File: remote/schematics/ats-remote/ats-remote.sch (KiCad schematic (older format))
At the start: 34 parts, among them J1 PWR, J2 ICSP, J3 Conn_01x04_Male, J4 Conn_01x02_Male, U1 RFM95W-915S2, U2 PIC18F06Q40, U3 YIC71009EBGG

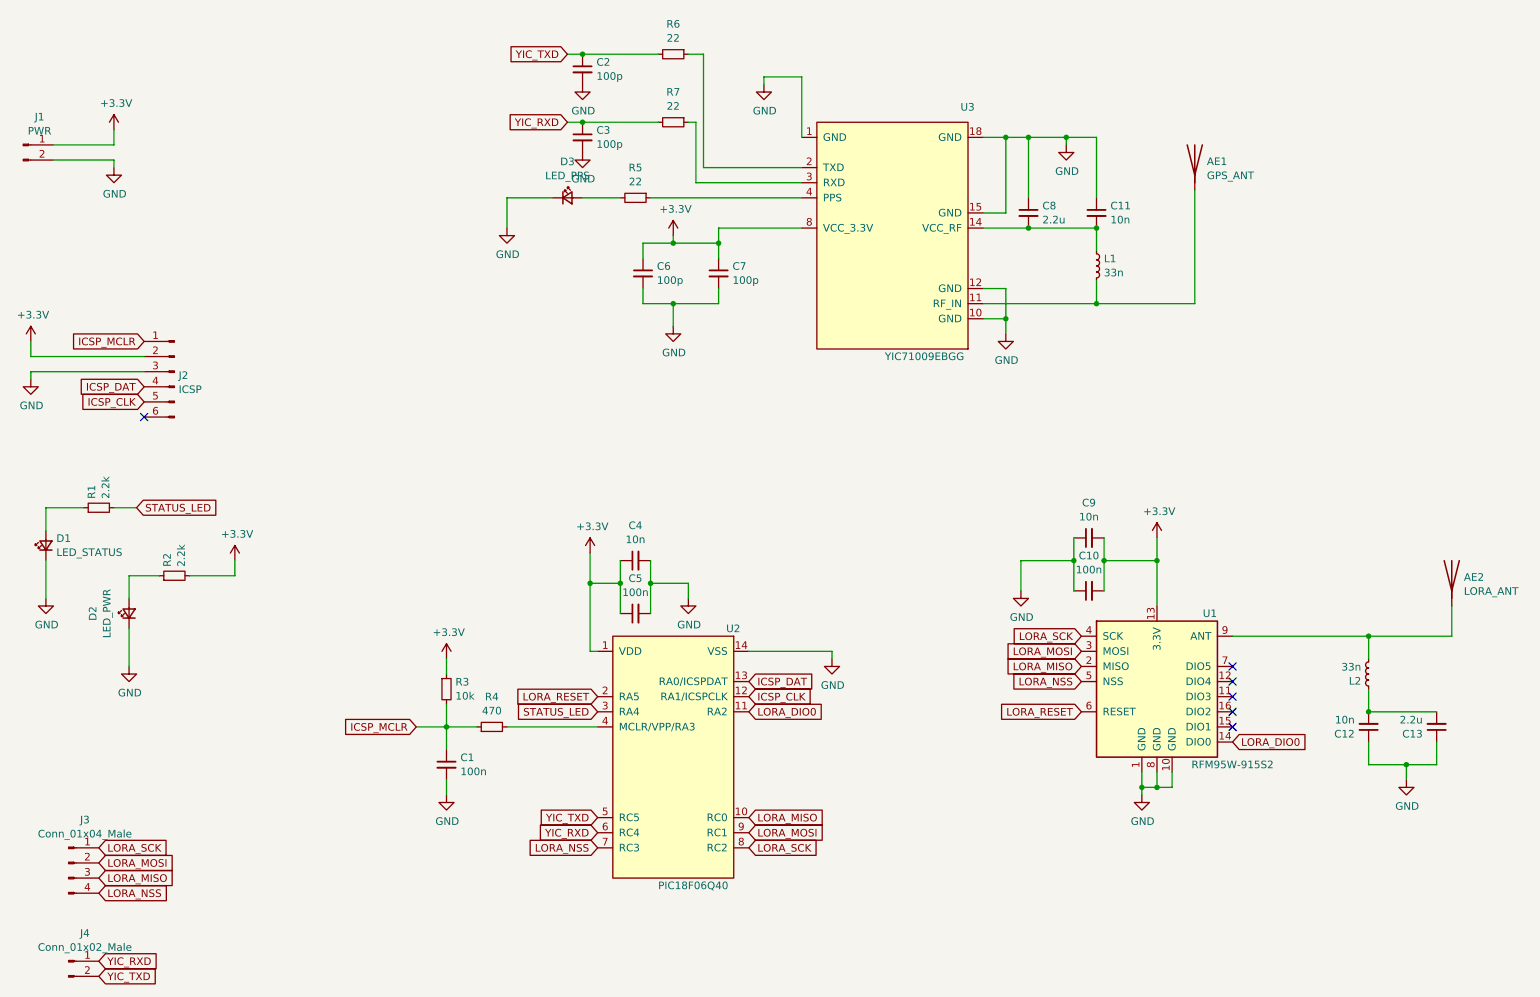
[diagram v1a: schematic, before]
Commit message: v0.2.1 (#3)
* add footprints for gps and lora antennas; start work on new board

* update schematic and pcb to v0.2.0

* Update README.md

* remove gerber files

* update schematic and pcb

* add silk screen

* update silk screen

* fix lora nss via and gps ant grounds
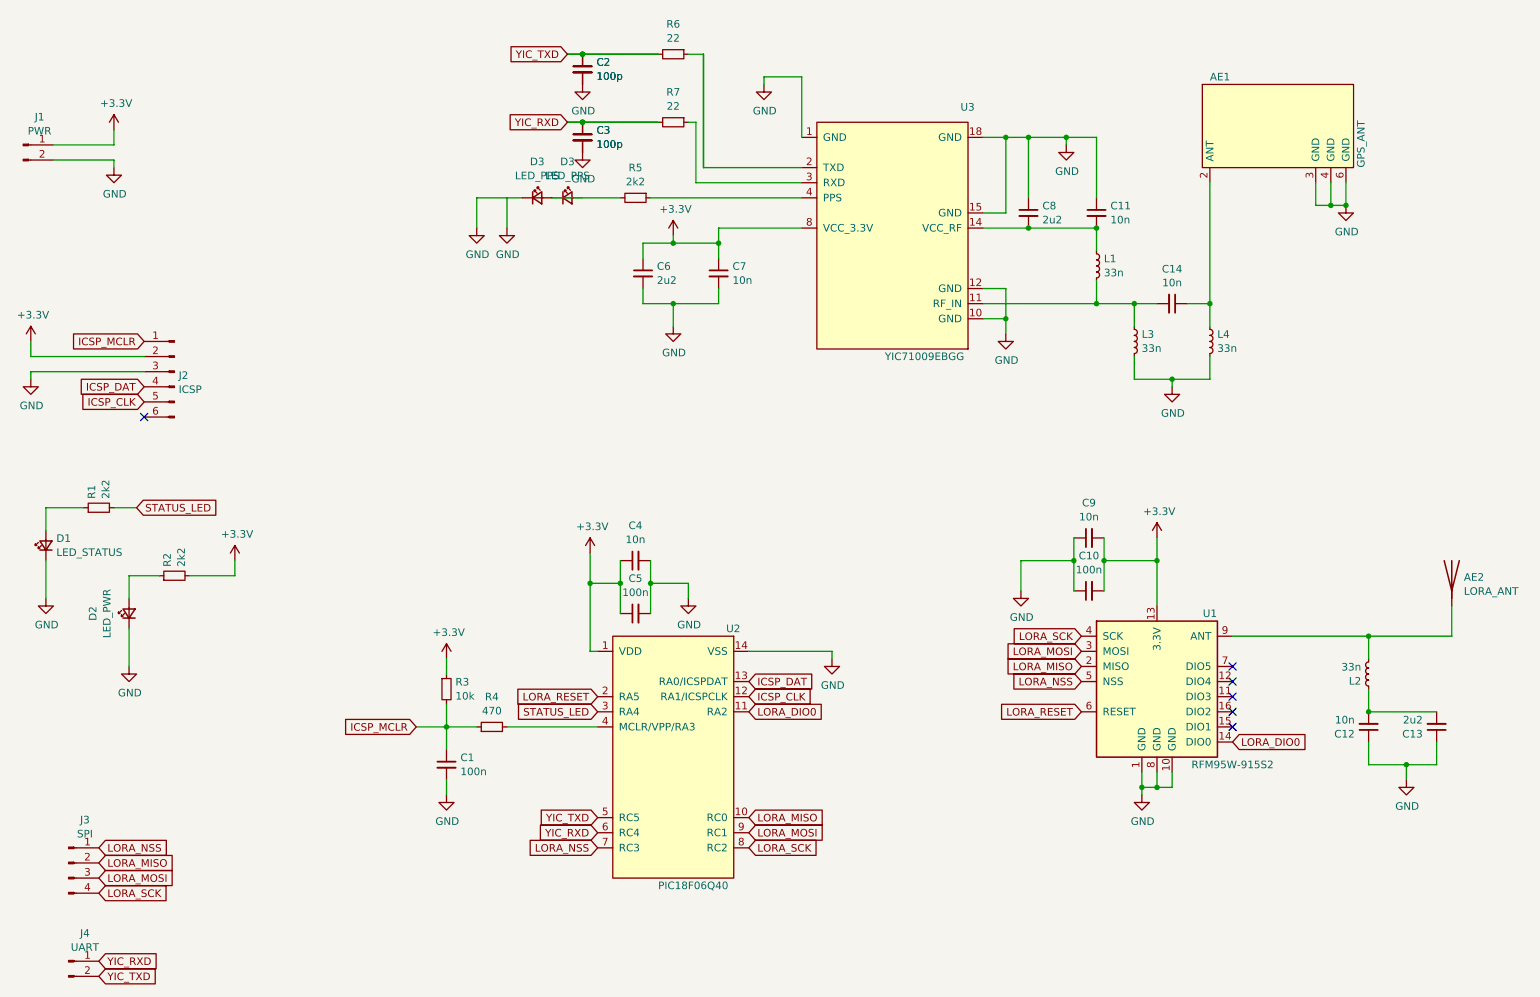
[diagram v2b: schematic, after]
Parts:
- removed AE1: GPS_ANT, ats-remote:GPS_ANT_SR4G008, symbol Device:Antenna
- removed D3: LED_PPS, Diode_SMD:D_1206_3216Metric_Pad1.42x1.75mm_HandSolder, symbol Device:LED_Small
- added AE1: GPS_ANT, ats-remote:GPS_ANT_SR4G008, symbol ats-remote:ACAG1204-915-T
- added C14: 10n, Capacitor_SMD:C_0805_2012Metric_Pad1.18x1.45mm_HandSolder, symbol Device:C_Small
- added D3 (x2): LED_PPS, Diode_SMD:D_1206_3216Metric_Pad1.42x1.75mm_HandSolder, symbol Device:LED_Small
- added L3, L4: 33n, Inductor_SMD:L_0603_1608Metric_Pad1.05x0.95mm_HandSolder, symbol Device:L_Small
- C13, C8: value 2.2u -> 2u2
- C6: value 100p -> 2u2
- C7: value 100p -> 10n
- J3: value Conn_01x04_Male -> SPI
- J4: value Conn_01x02_Male -> UART
- R1, R2: value 2.2k -> 2k2
- R5: value 22 -> 2k2
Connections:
- net GND: now also AE1.3 (GND), AE1.4 (GND), AE1.6 (GND), D3.1 (K), L3.2, L4.2
- net LORA_MISO: now also J3.2 (Pin_2); no longer J3.3 (Pin_3)
- net LORA_MOSI: now also J3.3 (Pin_3); no longer J3.2 (Pin_2)
- net LORA_NSS: now also J3.1 (Pin_1); no longer J3.4 (Pin_4)
- net LORA_SCK: now also J3.4 (Pin_4); no longer J3.1 (Pin_1)
- net at L1.2, U3.11 (RF_IN): now also C14.2, L3.1
- net at R5.2: now also D3.1 (K), D3.2 (A)
- new net: AE1.2 (ANT), C14.1, L4.1
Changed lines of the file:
@@
 	10100 4750 10100 4550
-$Comp
-L Device:Antenna AE1
-U 1 1 61DAE6EE
-P 8400 1600
-F 0 "AE1" H 8480 1590 50  0000 L CNN
-F 1 "GPS_ANT" H 8480 1497 50  0000 L CNN
-F 2 "ats-remote:GPS_ANT_SR4G008" H 8400 1600 50  0001 C CNN
-F 3 "~" H 8400 1600 50  0001 C CNN
-	1    8400 1600
-	1    0    0    -1
-$EndComp
 $Comp
 L Device:LED_Small D1
@@
 P 1150 3900
 F 0 "R1" H 1209 3947 50  0000 L CNN
-F 1 "2.2k" H 1209 3854 50  0000 L CNN
+F 1 "2k2" H 1209 3854 50  0000 L CNN
 F 2 "Resistor_SMD:R_1206_3216Metric_Pad1.30x1.75mm_HandSolder" H 1150 3900 50  0001 C CNN
 F 3 "~" H 1150 3900 50  0001 C CNN
@@
 P 1650 4350
 F 0 "R2" H 1709 4397 50  0000 L CNN
-F 1 "2.2k" H 1709 4304 50  0000 L CNN
+F 1 "2k2" H 1709 4304 50  0000 L CNN
 F 2 "Resistor_SMD:R_1206_3216Metric_Pad1.30x1.75mm_HandSolder" H 1650 4350 50  0001 C CNN
 F 3 "~" H 1650 4350 50  0001 C CNN
@@
 P 7300 1950
 F 0 "C8" H 7392 1997 50  0000 L CNN
-F 1 "2.2u" H 7392 1904 50  0000 L CNN
+F 1 "2u2" H 7392 1904 50  0000 L CNN
 F 2 "Capacitor_SMD:C_0805_2012Metric_Pad1.18x1.45mm_HandSolder" H 7300 1950 50  0001 C CNN
 F 3 "~" H 7300 1950 50  0001 C CNN
@@
 Wire Wire Line
 	7750 1450 7750 1850
-Wire Wire Line
-	8400 1800 8400 2550
 Wire Wire Line
 	7000 2550 7750 2550
@@
 Wire Wire Line
 	7750 2400 7750 2550
-Connection ~ 7750 2550
-Wire Wire Line
-	7750 2550 8400 2550
 Wire Wire Line
 	5800 1750 5100 1750
@@
 P 4700 1850
 F 0 "R5" V 4501 1850 50  0000 C CNN
-F 1 "22" V 4594 1850 50  0000 C CNN
+F 1 "2k2" V 4594 1850 50  0000 C CNN
 F 2 "Resistor_SMD:R_1206_3216Metric_Pad1.30x1.75mm_HandSolder" H 4700 1850 50  0001 C CNN
 F 3 "~" H 4700 1850 50  0001 C CNN
@@
 	0    1    1    0
 $EndComp
+Wire Wire Line
+	5150 900  5150 1650
+Wire Wire Line
+	4850 1350 4350 1350
+Wire Wire Line
+	4850 900  4350 900
+$Comp
+L power:GND #PWR0120
+U 1 1 61F19544
+P 3850 2050
+F 0 "#PWR0120" H 3850 1800 50  0001 C CNN
+F 1 "GND" H 3855 1875 50  0000 C CNN
+F 2 "" H 3850 2050 50  0001 C CNN
+F 3 "" H 3850 2050 50  0001 C CNN
+	1    3850 2050
+	1    0    0    -1
+$EndComp
+$Comp
+L Device:LED_Small D3
+U 1 1 61F1DC27
+P 4250 1850
+F 0 "D3" H 4250 2089 50  0000 C CNN
+F 1 "LED_PPS" H 4250 1996 50  0000 C CNN
+F 2 "Diode_SMD:D_1206_3216Metric_Pad1.42x1.75mm_HandSolder" V 4250 1850 50  0001 C CNN
+F 3 "~" V 4250 1850 50  0001 C CNN
+	1    4250 1850
+	1    0    0    -1
+$EndComp
+Wire Wire Line
+	3850 1850 3850 2050
+$Comp
+L Device:C_Small C3
+U 1 1 61F2C911
+P 4350 1450
+F 0 "C3" H 4442 1497 50  0000 L CNN
+F 1 "100p" H 4442 1404 50  0000 L CNN
+F 2 "Capacitor_SMD:C_0805_2012Metric_Pad1.18x1.45mm_HandSolder" H 4350 1450 50  0001 C CNN
+F 3 "~" H 4350 1450 50  0001 C CNN
+	1    4350 1450
+	1    0    0    -1
+$EndComp
+$Comp
+L Device:C_Small C2
+U 1 1 61F2ED54
+P 4350 1000
+F 0 "C2" H 4442 1047 50  0000 L CNN
+F 1 "100p" H 4442 954 50  0000 L CNN
+F 2 "Capacitor_SMD:C_0805_2012Metric_Pad1.18x1.45mm_HandSolder" H 4350 1000 50  0001 C CNN
+F 3 "~" H 4350 1000 50  0001 C CNN
+	1    4350 1000
+	1    0    0    -1
+$EndComp
+Connection ~ 4350 900
+Wire Wire Line
+	4350 900  4250 900
+Connection ~ 4350 1350
+Wire Wire Line
+	4350 1350 4250 1350
 $Comp
 L Device:R_Small R6
@@
 L power:GND #PWR0120
 U 1 1 61F19544
-P 3850 2050
-F 0 "#PWR0120" H 3850 1800 50  0001 C CNN
-F 1 "GND" H 3855 1875 50  0000 C CNN
-F 2 "" H 3850 2050 50  0001 C CNN
-F 3 "" H 3850 2050 50  0001 C CNN
-	1    3850 2050
+P 3650 2050
+F 0 "#PWR0120" H 3650 1800 50  0001 C CNN
+F 1 "GND" H 3655 1875 50  0000 C CNN
+F 2 "" H 3650 2050 50  0001 C CNN
+F 3 "" H 3650 2050 50  0001 C CNN
+	1    3650 2050
 	1    0    0    -1
 $EndComp
@@
 L Device:LED_Small D3
 U 1 1 61F1DC27
-P 4250 1850
-F 0 "D3" H 4250 2089 50  0000 C CNN
-F 1 "LED_PPS" H 4250 1996 50  0000 C CNN
-F 2 "Diode_SMD:D_1206_3216Metric_Pad1.42x1.75mm_HandSolder" V 4250 1850 50  0001 C CNN
-F 3 "~" V 4250 1850 50  0001 C CNN
-	1    4250 1850
-	1    0    0    -1
-$EndComp
-Wire Wire Line
-	3850 1850 3850 2050
+P 4050 1850
+F 0 "D3" H 4050 2089 50  0000 C CNN
+F 1 "LED_PPS" H 4050 1996 50  0000 C CNN
+F 2 "Diode_SMD:D_1206_3216Metric_Pad1.42x1.75mm_HandSolder" V 4050 1850 50  0001 C CNN
+F 3 "~" V 4050 1850 50  0001 C CNN
+	1    4050 1850
+	1    0    0    -1
+$EndComp
+Wire Wire Line
+	3650 1850 3650 2050
 $Comp
 L Device:C_Small C3
@@
 P 4750 2350
 F 0 "C6" H 4842 2397 50  0000 L CNN
-F 1 "100p" H 4842 2304 50  0000 L CNN
+F 1 "2u2" H 4842 2304 50  0000 L CNN
 F 2 "Capacitor_SMD:C_0805_2012Metric_Pad1.18x1.45mm_HandSolder" H 4750 2350 50  0001 C CNN
 F 3 "~" H 4750 2350 50  0001 C CNN
@@
 P 5250 2350
 F 0 "C7" H 5342 2397 50  0000 L CNN
-F 1 "100p" H 5342 2304 50  0000 L CNN
+F 1 "10n" H 5342 2304 50  0000 L CNN
 F 2 "Capacitor_SMD:C_0805_2012Metric_Pad1.18x1.45mm_HandSolder" H 5250 2350 50  0001 C CNN
 F 3 "~" H 5250 2350 50  0001 C CNN
@@
 P 10000 5350
 F 0 "C13" H 10092 5397 50  0000 L CNN
-F 1 "2.2u" H 10092 5304 50  0000 L CNN
+F 1 "2u2" H 10092 5304 50  0000 L CNN
 F 2 "Capacitor_SMD:C_0805_2012Metric_Pad1.18x1.45mm_HandSolder" H 10000 5350 50  0001 C CNN
 F 3 "~" H 10000 5350 50  0001 C CNN
@@
 LORA_RESET
 Wire Wire Line
-	3850 1850 4150 1850
-Wire Wire Line
-	4350 1850 4600 1850
+	3650 1850 3950 1850
 Wire Wire Line
 	800  4050 800  3900
@@
 P 950 6250
 F 0 "J3" H 1058 6535 50  0000 C CNN
-F 1 "Conn_01x04_Male" H 1058 6442 50  0000 C CNN
+F 1 "SPI" H 1058 6442 50  0000 C CNN
 F 2 "Connector_PinHeader_1.27mm:PinHeader_1x04_P1.27mm_Vertical" H 950 6250 50  0001 C CNN
 F 3 "~" H 950 6250 50  0001 C CNN
@@
 P 950 6900
 F 0 "J4" H 1058 7085 50  0000 C CNN
-F 1 "Conn_01x02_Male" H 1058 6992 50  0000 C CNN
+F 1 "UART" H 1058 6992 50  0000 C CNN
 F 2 "Connector_PinHeader_1.27mm:PinHeader_1x02_P1.27mm_Vertical" H 950 6900 50  0001 C CNN
 F 3 "~" H 950 6900 50  0001 C CNN
@@
 	1    0    0    -1
 $EndComp
+Text GLabel 1150 6450 2    50   Input ~ 0
+LORA_SCK
+Text GLabel 1150 6350 2    50   Input ~ 0
+LORA_MOSI
+Text GLabel 1150 6250 2    50   Input ~ 0
+LORA_MISO
 Text GLabel 1150 6150 2    50   Input ~ 0
-LORA_SCK
-Text GLabel 1150 6250 2    50   Input ~ 0
-LORA_MOSI
-Text GLabel 1150 6350 2    50   Input ~ 0
-LORA_MISO
-Text GLabel 1150 6450 2    50   Input ~ 0
 LORA_NSS
 Text GLabel 1150 7000 2    50   Input ~ 0
@@
 Text GLabel 1150 6900 2    50   Input ~ 0
 YIC_RXD
+Wire Wire Line
+	4150 1850 4600 1850
+$Comp
+L Device:C_Small C14
+U 1 1 61CC5279
+P 8250 2550
+F 0 "C14" V 8021 2550 50  0000 C CNN
+F 1 "10n" V 8112 2550 50  0000 C CNN
+F 2 "Capacitor_SMD:C_0805_2012Metric_Pad1.18x1.45mm_HandSolder" H 8250 2550 50  0001 C CNN
+F 3 "~" H 8250 2550 50  0001 C CNN
+	1    8250 2550
+	0    1    1    0
+$EndComp
+$Comp
+L Device:L_Small L3
+U 1 1 61CC7ED4
+P 8000 2800
+F 0 "L3" H 8049 2847 50  0000 L CNN
+F 1 "33n" H 8049 2754 50  0000 L CNN
+F 2 "Inductor_SMD:L_0603_1608Metric_Pad1.05x0.95mm_HandSolder" H 8000 2800 50  0001 C CNN
+F 3 "~" H 8000 2800 50  0001 C CNN
+	1    8000 2800
+	1    0    0    -1
+$EndComp
+Wire Wire Line
+	8000 2900 8000 3050
+$Comp
+L Device:L_Small L4
+U 1 1 61CCBBC5
+P 8500 2800
+F 0 "L4" H 8549 2847 50  0000 L CNN
+F 1 "33n" H 8549 2754 50  0000 L CNN
+F 2 "Inductor_SMD:L_0603_1608Metric_Pad1.05x0.95mm_HandSolder" H 8500 2800 50  0001 C CNN
+F 3 "~" H 8500 2800 50  0001 C CNN
+	1    8500 2800
+	1    0    0    -1
+$EndComp
+Wire Wire Line
+	8500 2900 8500 3050
+Wire Wire Line
+	7750 2550 8000 2550
+Connection ~ 7750 2550
+Wire Wire Line
+	8000 2700 8000 2550
+Connection ~ 8000 2550
+Wire Wire Line
+	8000 2550 8150 2550
+$Comp
+L power:GND #PWR0125
+U 1 1 61CE9263
+P 8250 3100
+F 0 "#PWR0125" H 8250 2850 50  0001 C CNN
+F 1 "GND" H 8255 2925 50  0000 C CNN
+F 2 "" H 8250 3100 50  0001 C CNN
+F 3 "" H 8250 3100 50  0001 C CNN
+	1    8250 3100
+	1    0    0    -1
+$EndComp
+Wire Wire Line
+	8000 3050 8250 3050
+Wire Wire Line
+	8250 3050 8250 3100
+Wire Wire Line
+	8250 3050 8500 3050
+Connection ~ 8250 3050
+$Comp
+L ats-remote:ACAG1204-915-T AE1
+U 1 1 61D69634
+P 8950 1400
+F 0 "AE1" H 8500 1750 50  0000 L CNN
+F 1 "GPS_ANT" V 9500 1150 50  0000 L CNN
+F 2 "ats-remote:GPS_ANT_SR4G008" H 8950 2450 50  0001 C CNN
+F 3 "" H 8950 2450 50  0001 C CNN
+	1    8950 1400
+	1    0    0    -1
+$EndComp
+$Comp
+L power:GND #PWR0126
+U 1 1 61D7E716
+P 9400 1900
+F 0 "#PWR0126" H 9400 1650 50  0001 C CNN
+F 1 "GND" H 9405 1725 50  0000 C CNN
+F 2 "" H 9400 1900 50  0001 C CNN
+F 3 "" H 9400 1900 50  0001 C CNN
+	1    9400 1900
+	1    0    0    -1
+$EndComp
+Wire Wire Line
+	9200 1750 9200 1900
+Wire Wire Line
+	9200 1900 9300 1900
+Wire Wire Line
+	9300 1750 9300 1900
+Connection ~ 9300 1900
+Wire Wire Line
+	9300 1900 9400 1900
+Wire Wire Line
+	9400 1750 9400 1900
+Connection ~ 9400 1900
+Wire Wire Line
+	8350 2550 8500 2550
+Wire Wire Line
+	8500 2550 8500 1750
+Wire Wire Line
+	8500 2550 8500 2700
+Connection ~ 8500 2550
 $EndSCHEMATC

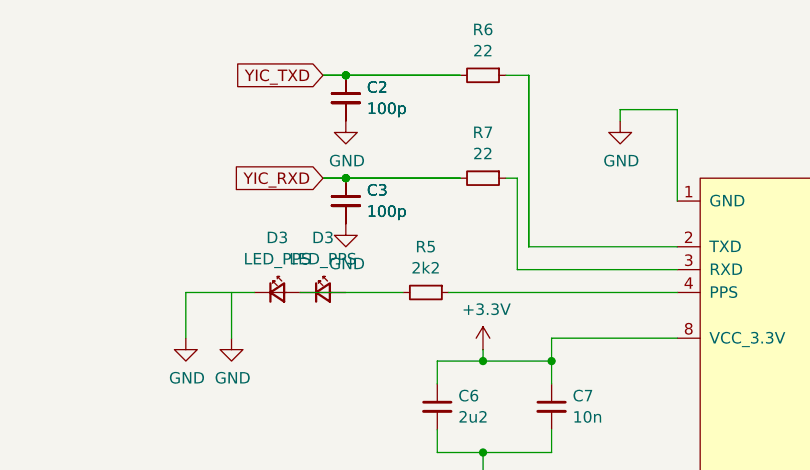
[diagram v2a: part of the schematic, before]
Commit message: update spi drivers to fix several bugs and add tmr0 interrupt handler for status led
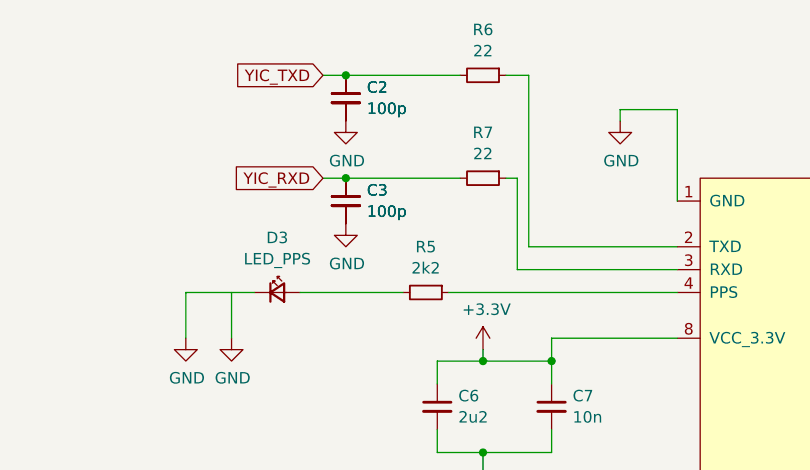
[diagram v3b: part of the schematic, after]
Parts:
- removed D3 (x2): LED_PPS, Diode_SMD:D_1206_3216Metric_Pad1.42x1.75mm_HandSolder, symbol Device:LED_Small
- added D3: LED_PPS, Diode_SMD:D_1206_3216Metric_Pad1.42x1.75mm_HandSolder, symbol Device:LED_Small
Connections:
- net GND: now also D3.1 (K)
- net at R5.2: now also D3.2 (A)
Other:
- moved on the sheet: D3
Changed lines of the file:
@@
-	1    0    0    -1
-$EndComp
-$Comp
-L Device:LED_Small D3
-U 1 1 61F1DC27
-P 4250 1850
-F 0 "D3" H 4250 2089 50  0000 C CNN
-F 1 "LED_PPS" H 4250 1996 50  0000 C CNN
-F 2 "Diode_SMD:D_1206_3216Metric_Pad1.42x1.75mm_HandSolder" V 4250 1850 50  0001 C CNN
-F 3 "~" V 4250 1850 50  0001 C CNN
-	1    4250 1850
 	1    0    0    -1
 $EndComp
@@
 	0    1    1    0
 $EndComp
-Wire Wire Line
-	5150 900  5150 1650
-Wire Wire Line
-	4850 1350 4350 1350
-Wire Wire Line
-	4850 900  4350 900
 $Comp
 L power:GND #PWR0120
@@
 	1    0    0    -1
 $EndComp
-Connection ~ 4350 900
-Wire Wire Line
-	4350 900  4250 900
-Connection ~ 4350 1350
-Wire Wire Line
-	4350 1350 4250 1350
 $Comp
 L ats-remote:YIC71009EBGG U3
@@
 Text GLabel 1150 6900 2    50   Input ~ 0
 YIC_RXD
-Wire Wire Line
-	4150 1850 4600 1850
 $Comp
 L Device:C_Small C14
@@
 	8500 2550 8500 2700
 Connection ~ 8500 2550
+Wire Wire Line
+	4150 1850 4600 1850
 $EndSCHEMATC

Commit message: update resistor values to reflect those used on board
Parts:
- R1, R2, R5: value 2k2 -> 3k3
- R4: value 470 -> 510
- R6, R7: value 22 -> 33
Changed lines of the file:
@@
 P 1150 3900
 F 0 "R1" H 1209 3947 50  0000 L CNN
-F 1 "2k2" H 1209 3854 50  0000 L CNN
+F 1 "3k3" H 1209 3854 50  0000 L CNN
 F 2 "Resistor_SMD:R_1206_3216Metric_Pad1.30x1.75mm_HandSolder" H 1150 3900 50  0001 C CNN
 F 3 "~" H 1150 3900 50  0001 C CNN
@@
 P 3750 5350
 F 0 "R4" V 3949 5350 50  0000 C CNN
-F 1 "470" V 3856 5350 50  0000 C CNN
+F 1 "510" V 3856 5350 50  0000 C CNN
 F 2 "Resistor_SMD:R_1206_3216Metric_Pad1.30x1.75mm_HandSolder" H 3809 5257 50  0001 L CNN
 F 3 "~" H 3750 5350 50  0001 C CNN
@@
 P 1650 4350
 F 0 "R2" H 1709 4397 50  0000 L CNN
-F 1 "2k2" H 1709 4304 50  0000 L CNN
+F 1 "3k3" H 1709 4304 50  0000 L CNN
 F 2 "Resistor_SMD:R_1206_3216Metric_Pad1.30x1.75mm_HandSolder" H 1650 4350 50  0001 C CNN
 F 3 "~" H 1650 4350 50  0001 C CNN
@@
 P 4700 1850
 F 0 "R5" V 4501 1850 50  0000 C CNN
-F 1 "2k2" V 4594 1850 50  0000 C CNN
+F 1 "3k3" V 4594 1850 50  0000 C CNN
 F 2 "Resistor_SMD:R_1206_3216Metric_Pad1.30x1.75mm_HandSolder" H 4700 1850 50  0001 C CNN
 F 3 "~" H 4700 1850 50  0001 C CNN
@@
 P 4950 1350
 F 0 "R7" V 4751 1350 50  0000 C CNN
-F 1 "22" V 4844 1350 50  0000 C CNN
+F 1 "33" V 4844 1350 50  0000 C CNN
 F 2 "Resistor_SMD:R_1206_3216Metric_Pad1.30x1.75mm_HandSolder" H 4950 1350 50  0001 C CNN
 F 3 "~" H 4950 1350 50  0001 C CNN
@@
 P 4950 900
 F 0 "R6" V 4751 900 50  0000 C CNN
-F 1 "22" V 4844 900 50  0000 C CNN
+F 1 "33" V 4844 900 50  0000 C CNN
 F 2 "Resistor_SMD:R_1206_3216Metric_Pad1.30x1.75mm_HandSolder" H 4950 900 50  0001 C CNN
 F 3 "~" H 4950 900 50  0001 C CNN
